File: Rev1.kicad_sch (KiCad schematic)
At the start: 14 parts, among them J1 Screw_Terminal_01x02, J2 AVR-ISP-6, J3 UART Debug, J4 OLED I2C, U2 ProMicro

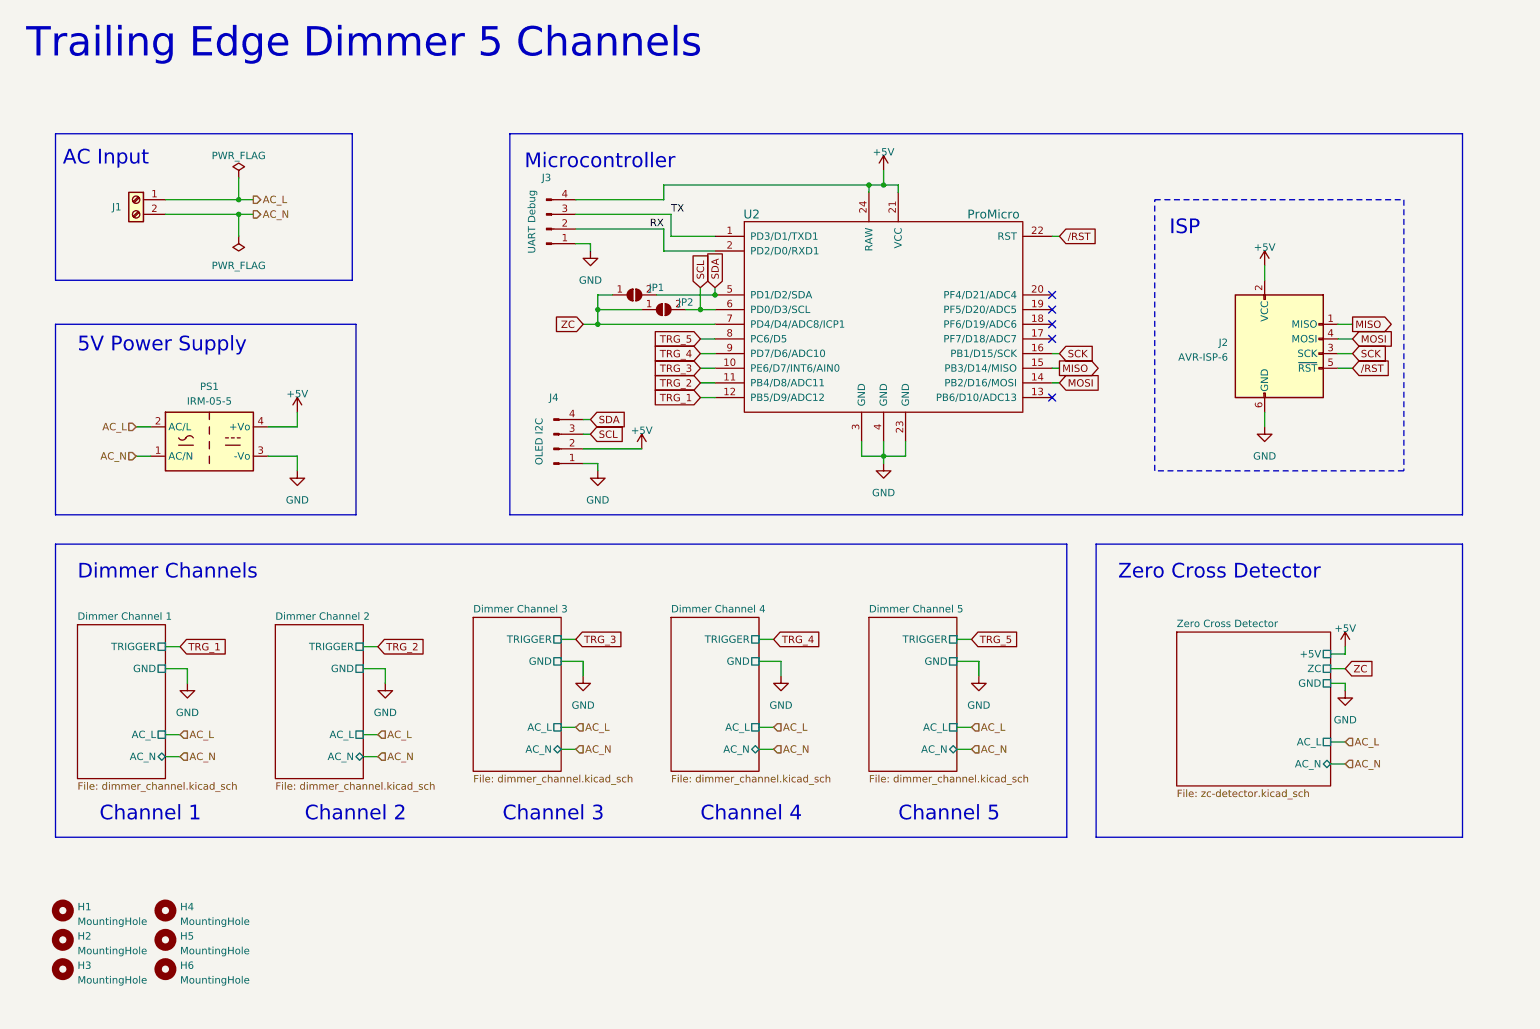
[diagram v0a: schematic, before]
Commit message: Added changes based on Tim Williams feedback on StackExchange.
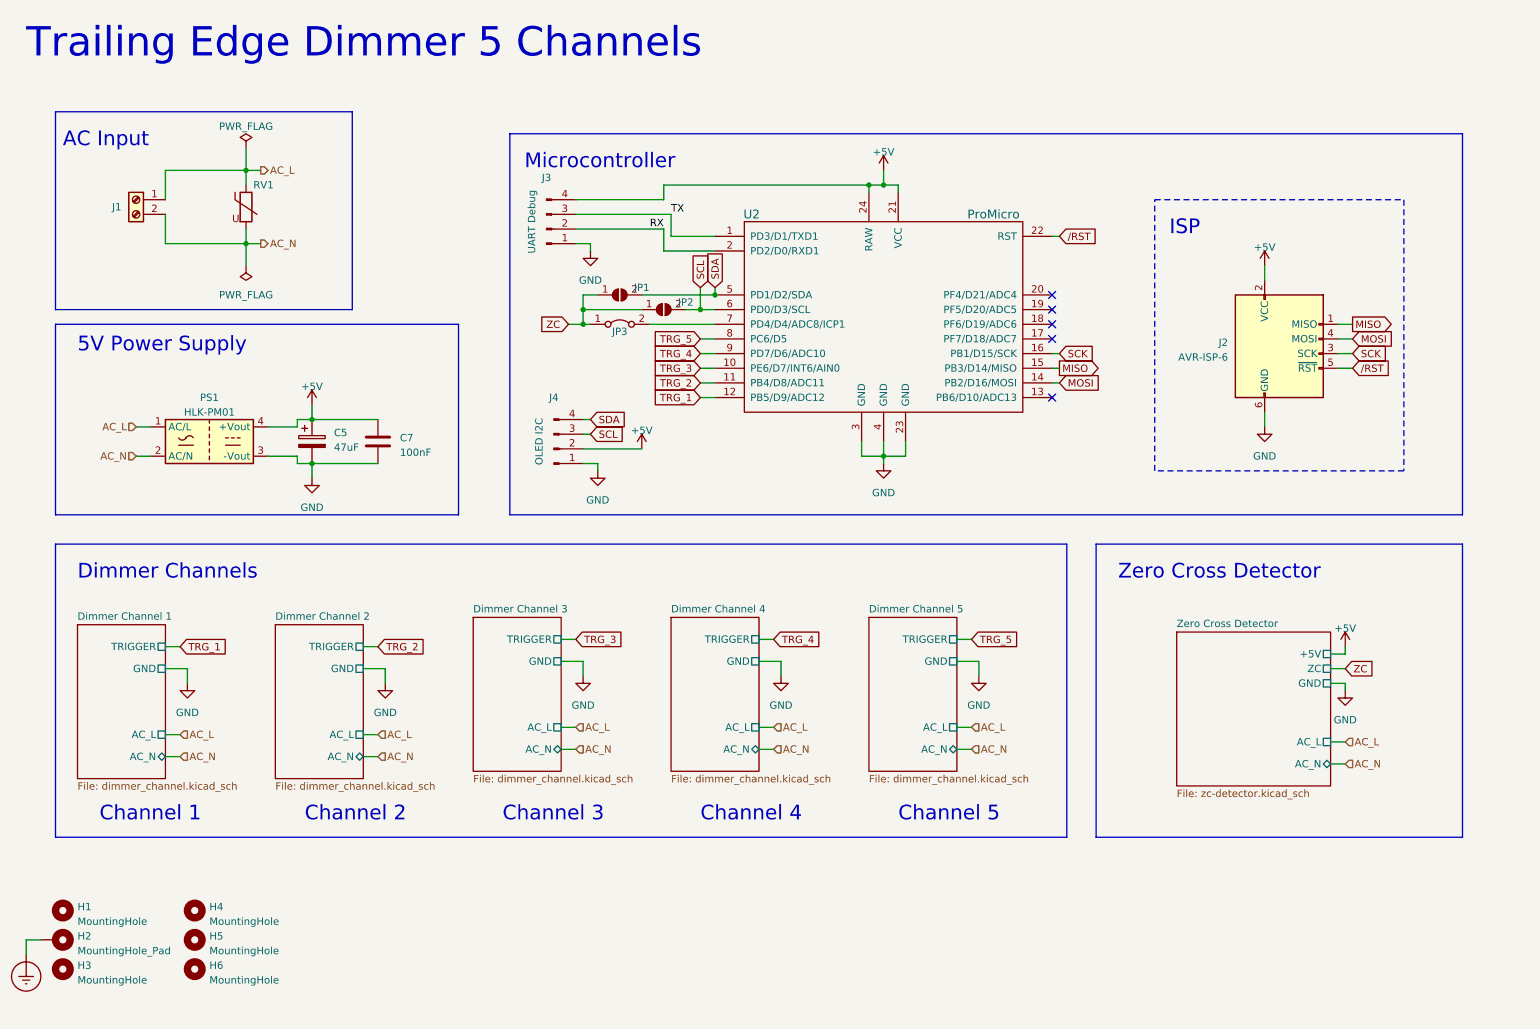
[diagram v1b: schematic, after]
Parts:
- removed H2: MountingHole, MountingHole:MountingHole_3.2mm_M3_DIN965_Pad, symbol Mechanical:MountingHole
- removed PS1: IRM-05-5, Converter_ACDC:Converter_ACDC_MeanWell_IRM-05-xx_THT, symbol Converter_ACDC:IRM-05-5
- added C5: 47uF, Capacitor_SMD:CP_Elec_6.3x5.4, symbol Device:C_Polarized
- added C7: 100nF, Capacitor_SMD:C_0805_2012Metric, symbol Device:C
- added H2: MountingHole_Pad, MountingHole:MountingHole_3.2mm_M3_DIN965_Pad, symbol Mechanical:MountingHole_Pad
- added JP3: ICP1, Jumper:SolderJumper-2_P1.3mm_Bridged2Bar_RoundedPad1.0x1.5mm, symbol Jumper:Jumper_2_Bridged
- added PS1: HLK-PM01, Converter_ACDC:Converter_ACDC_HiLink_HLK-PMxx, symbol Converter_ACDC:HLK-PM01
- added RV1: RM10D201KD1IE100, Varistor:RV_Disc_D12mm_W3.9mm_P7.5mm, symbol Device:Varistor
- H1, H3, H4, H5, H6: footprint MountingHole:MountingHole_3.2mm_M3_DIN965_Pad -> MountingHole:MountingHole_3.2mm_M3_DIN965
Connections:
- net +5V: now also C5.1, C7.1, PS1.4 (+Vout)
- net AC_L: now also PS1.1 (AC/L), RV1.1
- net AC_N: now also PS1.2 (AC/N), RV1.2
- net GND: now also C5.2, C7.2, PS1.3 (-Vout)
- net ZC: now also JP3.1 (A); no longer U2.7 (PD4/D4/ADC8/ICP1)
- new net: JP3.2 (B), U2.7 (PD4/D4/ADC8/ICP1)
- new net Earth_Protective: H2.1
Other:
- moved on the sheet: H4, H5, H6, JP1

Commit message: Added some test points. Added RS-485 Module. Updated PBC.
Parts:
- removed J4: OLED I2C, Connector_PinHeader_2.54mm:PinHeader_1x04_P2.54mm_Vertical, symbol Connector:Conn_01x04_Pin
- added H7: MountingHole, MountingHole:MountingHole_3.2mm_M3_DIN965, symbol Mechanical:MountingHole
- added TP1, TP2, TP3, TP4, TP5: TestPoint, TestPoint:TestPoint_THTPad_D2.0mm_Drill1.0mm, symbol Connector:TestPoint
- added TP6: TestPointZC, TestPoint:TestPoint_THTPad_D2.0mm_Drill1.0mm, symbol Connector:TestPoint
- added U8: RS485_MODULE, 0x3333:RS485_MODULE, symbol 0x3333:RS485_MODULE
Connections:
- net +5V: now also U8.4 (VCC)
- net GND: now also U8.1 (GND)
- net RX: now also U8.5 (RO)
- net TRG_1: now also TP1.1
- net TRG_2: now also TP2.1
- net TRG_3: now also TP3.1
- net TRG_4: now also TP4.1
- net TRG_5: now also TP5.1
- net TX: now also U8.8 (DI)
- net ZC: now also TP6.1
- net ME: now reaches U2.17 (PF7/D18/ADC7)
- net ME: now also U8.6 (~{RE}), U8.7 (DE)
- no-connect marks 5 -> 6
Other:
- note added: "RS-485"
- moved on the sheet: C5, C7, J2, J3, JP1, JP2, JP3, PS1, U2
